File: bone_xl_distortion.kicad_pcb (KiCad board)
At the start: 2 copper layers, 35 parts, among them J1 AudioJack2, J2 AudioJack2, U1 LM358, U2 J201

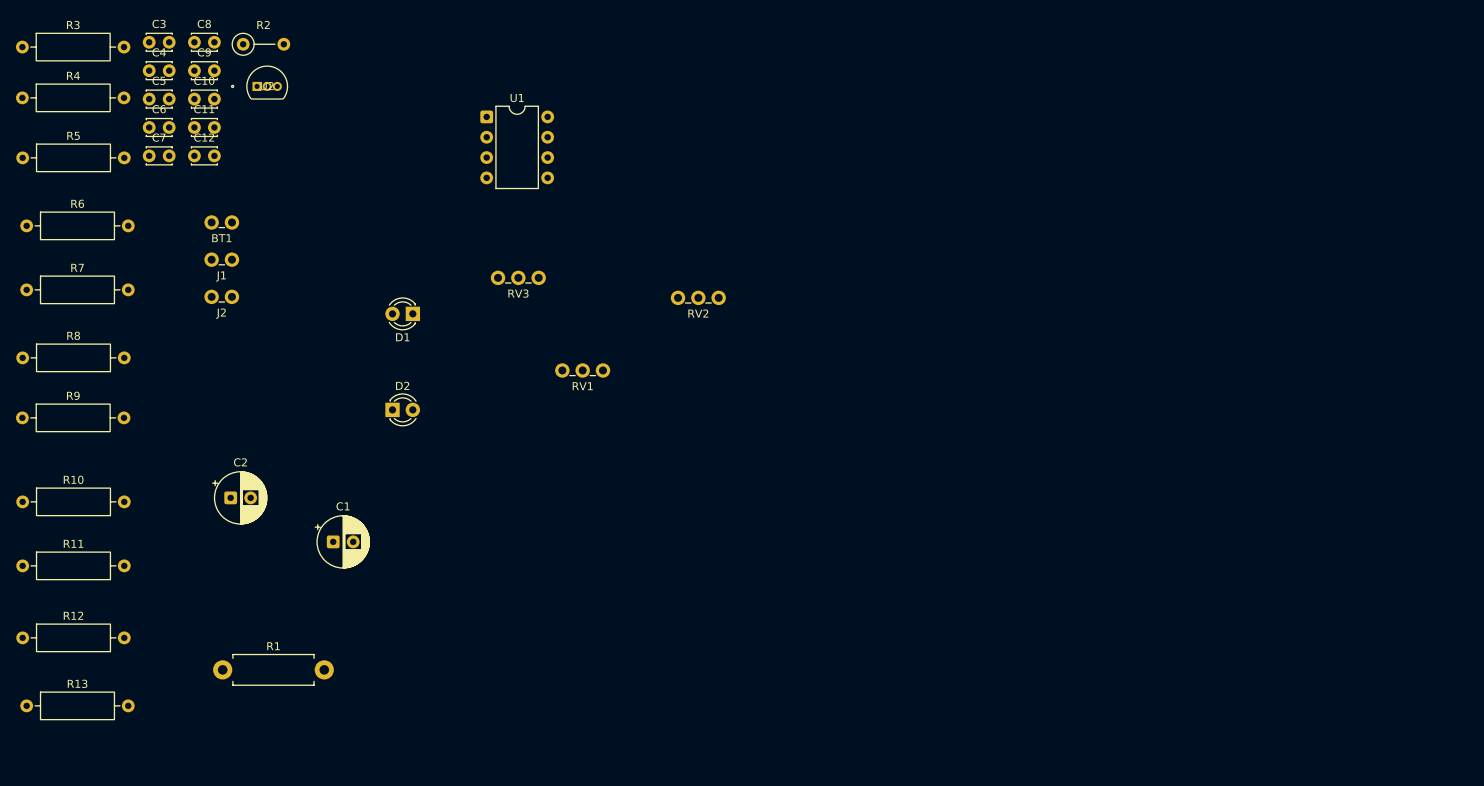
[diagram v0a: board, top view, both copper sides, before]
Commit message: finish pcb design minus silkscreen clipping and manufacturer board settings
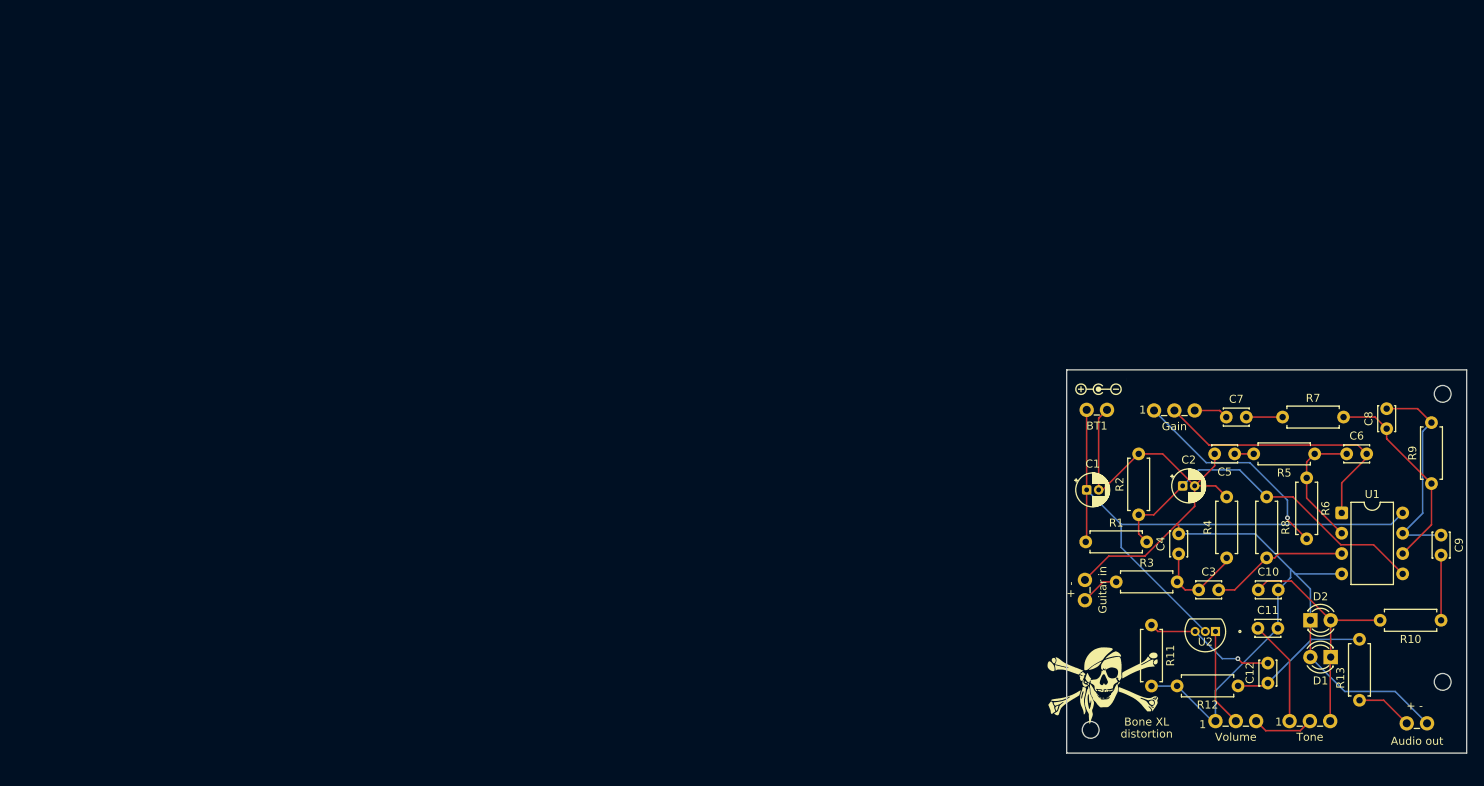
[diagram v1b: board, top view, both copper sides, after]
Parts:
- removed J1, J2: AudioJack2, standard_symbols:THT_Wire_Holes_x2
- removed RV1, RV3: 100kΩ, standard_symbols:THT_Wire_Holes_x3
- removed RV2: 10kΩ, standard_symbols:THT_Wire_Holes_x3
- added + -: Text, standard_symbols:text, F.Cu at (193.5, 110.0)
- added + -: Text, standard_symbols:text, F.Cu at (151.0, 95.0)
- added 1: Text, standard_symbols:text, F.Cu at (176.5, 112.0)
- added 1: Text, standard_symbols:text, F.Cu at (167.0, 112.3)
- added 1: Text, standard_symbols:text, F.Cu at (161.0, 71.0)
- added Audio out: AudioJack2, standard_symbols:THT_Offboard_Audio, F.Cu at (193.8, 114.4)
- added BONE XL: Text, standard_symbols:text, B.Cu at (176.5, 104.5)
- added Bone XL: Text, standard_symbols:text, F.Cu at (160.0, 112.0)
- added G***: LOGO, standard_symbols:negative_power, F.Cu at (154.0, 70.0)
- added G***: LOGO, standard_symbols:bone_logo_10mm, F.Cu at (154.5, 107.0)
- added G***: LOGO, standard_symbols:bone_logo_silk_screen, B.Cu at (175.5, 86.5)
- added G***: LOGO, standard_symbols:bone_xl_qr_silkscreen, B.Cu at (155.5, 105.0)
- added Gain: 100kΩ, standard_symbols:THT_Wire_Holes_x3, F.Cu at (163.5, 75.1)
- added Guitar in: AudioJack2, standard_symbols:THT_Offboard_Audio, F.Cu at (155.0, 95.0)
- added REF**: MountingHole_2.1mm, MountingHole:MountingHole_2.1mm, F.Cu at (197.0, 106.5)
- added REF**: MountingHole_2.1mm, MountingHole:MountingHole_2.1mm, F.Cu at (197.0, 70.5)
- added Tone: 10kΩ, standard_symbols:THT_Wire_Holes_x3, F.Cu at (180.4, 113.9)
- added Volume: 100kΩ, standard_symbols:THT_Wire_Holes_x3, F.Cu at (171.1, 113.9)
- added distortion: Text, standard_symbols:text, F.Cu at (160.0, 113.5)
- added https://github.com/delboy1978uk/bone-xl-distortion: Text, standard_symbols:text, B.Cu at (178.0, 114.0)
- added mount hole: MountingHole_2.1mm, MountingHole:MountingHole_2.1mm, F.Cu at (153.0, 112.5)
- C1, C2: footprint Capacitor_THT:CP_Radial_D6.3mm_P2.50mm -> Capacitor_THT:CP_Radial_D4.0mm_P1.50mm
- R1: footprint Resistor_THT:R_Axial_DIN0411_L9.9mm_D3.6mm_P12.70mm_Horizontal -> Resistor_THT:R_Axial_DIN0207_L6.3mm_D2.5mm_P7.62mm_Horizontal
- R10, R11, R12, R13, R3, R4, R5, R6, R7, R8, R9: footprint Resistor_THT:R_Axial_DIN0309_L9.0mm_D3.2mm_P12.70mm_Horizontal -> Resistor_THT:R_Axial_DIN0207_L6.3mm_D2.5mm_P7.62mm_Horizontal
- R2: footprint Resistor_THT:R_Axial_DIN0207_L6.3mm_D2.5mm_P5.08mm_Vertical -> Resistor_THT:R_Axial_DIN0207_L6.3mm_D2.5mm_P7.62mm_Horizontal
- moved R10 177.9 mm to (196.8, 98.8), turned to 180 degrees
- moved R9 176.3 mm to (195.6, 81.7), turned to 90 degrees
- moved R13 166.6 mm to (186.6, 108.8), turned to 90 degrees
- moved C9 166.3 mm to (196.8, 88.2), turned to -90 degrees
- moved R5 165.7 mm to (181.0, 78.0), turned to 180 degrees
- moved R6 163.1 mm to (180.0, 81.0), turned to -90 degrees
- moved R4 161.1 mm to (170.0, 91.0), turned to 90 degrees
- moved R7 157.8 mm to (177.0, 73.4)
- moved C8 156.7 mm to (190.0, 74.8), turned to 90 degrees
- moved R8 156.5 mm to (175.0, 83.4), turned to -90 degrees
- moved C6 155.1 mm to (185.0, 78.0)
- moved R3 152.2 mm to (156.2, 94.0)
- moved R12 152.0 mm to (171.4, 107.0), turned to 180 degrees
- moved C12 149.5 mm to (175.2, 106.7), turned to 90 degrees
- moved C3 148.0 mm to (166.5, 95.0)
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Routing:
- net GND: track 0.00 -> 141.7 mm
- net VCC: track 0.00 -> 76.2 mm
- net /Vref: track 0.00 -> 44.5 mm
- net Net-(C6-Pad2): track 0.00 -> 35.0 mm
- net Net-(D1-K): track 0.00 -> 30.4 mm
- net Net-(R6-Pad2): track 0.00 -> 27.1 mm, vias 0 -> 1
- net Net-(C8-Pad2): track 0.00 -> 26.5 mm
- net Net-(U1B--): track 0.00 -> 25.4 mm
- net Net-(C12-Pad1): track 0.00 -> 17.6 mm
- net Net-(U1A-+): track 0.00 -> 17.3 mm
- net Net-(U2-G): track 0.00 -> 16.5 mm, vias 0 -> 1
- net Net-(U1A--): track 0.00 -> 16.1 mm
- net Net-(C11-Pad1): track 0.00 -> 13.2 mm
- net Net-(U2-D): track 0.00 -> 12.3 mm
- net Net-(C3-Pad1): track 0.00 -> 12.1 mm
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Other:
- board outline added: 50 x 47.9 mm

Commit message: add PCBWay product marker
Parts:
- added WayWayWay: Text, standard_symbols:text, F.Cu at (179.5, 116.0)
- moved REF** 12.7 mm to (187.0, 114.4)
- moved mount hole 1.50 mm to (153.0, 114.0)
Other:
- board size 50 x 47.9 mm -> 50 x 50 mm
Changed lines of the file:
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@@
 	(footprint "MountingHole:MountingHole_2.1mm"
 		(layer "F.Cu")
-		(at 197 106.5)
+		(at 187 114.4)
 		(descr "Mounting Hole 2.1mm, no annular, generated by kicad-footprint-generator mountinghole.py")
 		(tags "mountinghole")
@@
 		(embedded_fonts no)
 	)
+	(footprint "standard_symbols:text"
+		(layer "F.Cu")
+		(at 179.5 116)
+		(property "Reference" "WayWayWay"
+			(at 0 -0.5 0)
+			(unlocked yes)
+			(layer "B.SilkS")
+			(effects
+				(font
+					(size 1 1)
+					(thickness 0.1)
+				)
+				(justify mirror)
+			)
+		)
+		(property "Value" "Text"
+			(at 0 1 0)
+			(unlocked yes)
+			(layer "F.Fab")
+			(effects
+				(font
+					(size 1 1)
+					(thickness 0.15)
+				)
+			)
+		)
+		(property "Datasheet" ""
+			(at 0 0 0)
+			(unlocked yes)
+			(layer "F.Fab")
+			(hide yes)
+			(effects
+				(font
+					(size 1 1)
+					(thickness 0.15)
+				)
+			)
+		)
+		(property "Description" ""
+			(at 0 0 0)
+			(unlocked yes)
+			(layer "F.Fab")
+			(hide yes)
+			(effects
+				(font
+					(size 1 1)
+					(thickness 0.15)
+				)
+			)
+		)
+		(attr board_only exclude_from_pos_files exclude_from_bom)
+		(fp_text user "${REFERENCE}"
+			(at 0 2.5 0)
+			(unlocked yes)
+			(layer "F.Fab")
+			(effects
+				(font
+					(size 1 1)
+					(thickness 0.15)
+				)
+			)
+		)
+		(embedded_fonts no)
+	)
 	(footprint "standard_symbols:THT_Wire_Holes_x3"
 		(layer "F.Cu")
@@
 	(footprint "MountingHole:MountingHole_2.1mm"
 		(layer "F.Cu")
-		(at 153 112.5)
+		(at 153 114)
 		(descr "Mounting Hole 2.1mm, no annular, generated by kicad-footprint-generator mountinghole.py")
 		(tags "mountinghole")
@@
 	(gr_rect
 		(start 150 67.5)
-		(end 200 115.4)
+		(end 200 117.5)
 		(stroke
 			(width 0.05)

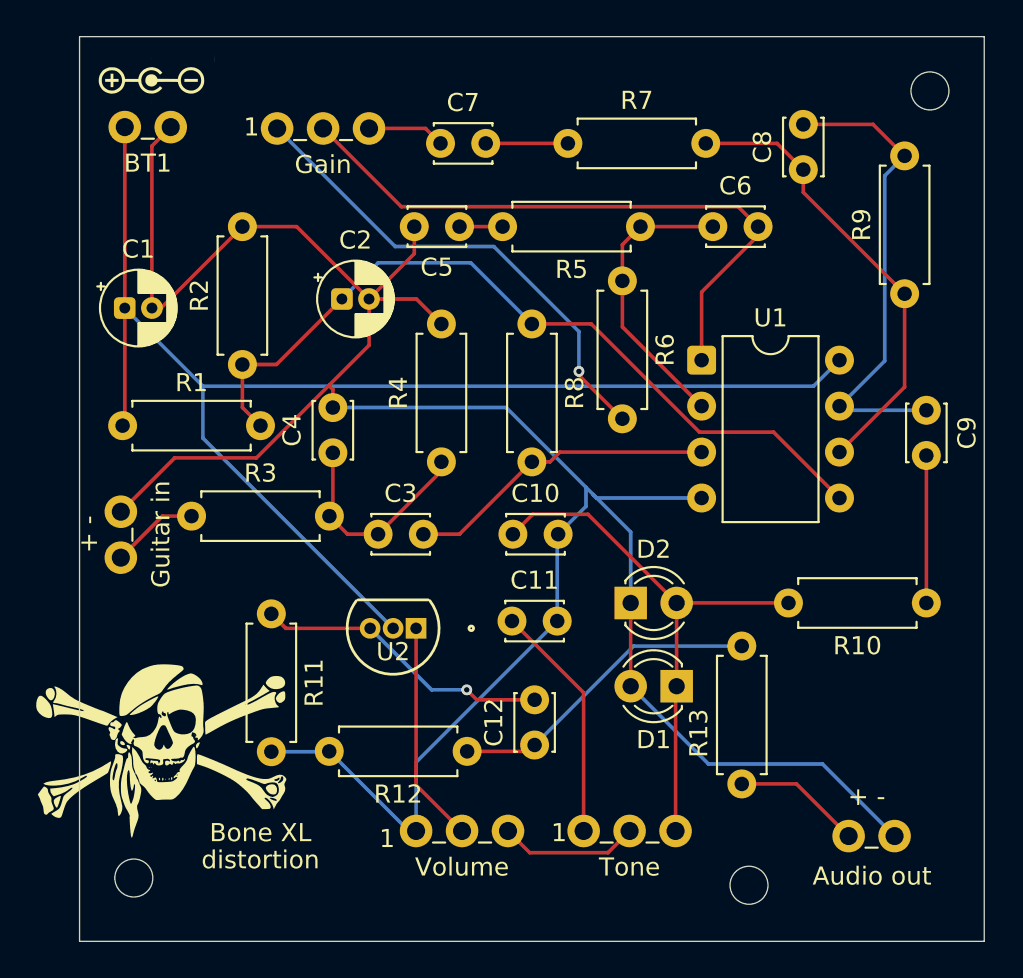
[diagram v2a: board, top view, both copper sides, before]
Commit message: add copper zones
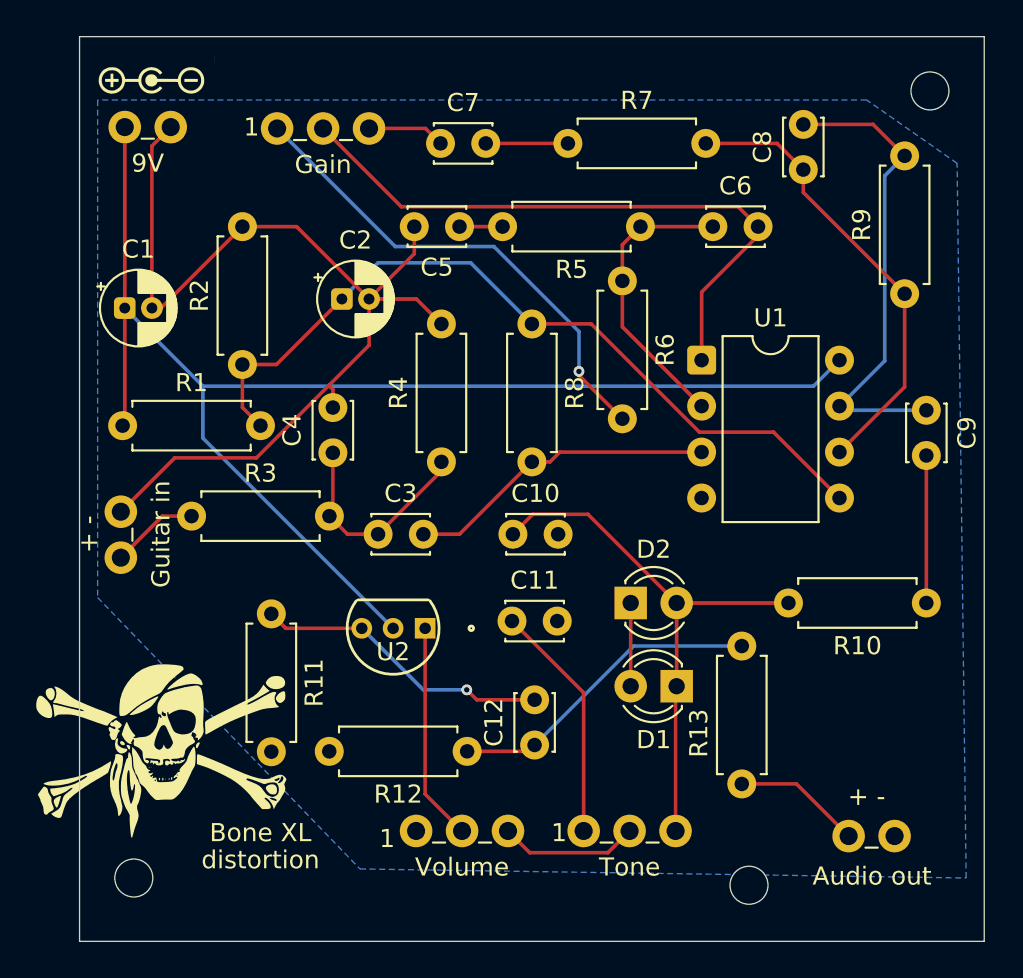
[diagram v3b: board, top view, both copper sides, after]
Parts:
- renumbered BT1 to 9V
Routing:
- net GND: track 141.7 -> 62.2 mm
- added copper zone on B.Cu, net GND
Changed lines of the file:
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@@
 		)
 		(pad "1" thru_hole rect
-			(at 0 0 180)
+			(at -0.5 0 180)
 			(size 1.143 1.143)
 			(drill 0.635)
@@
 		)
 		(pad "3" thru_hole circle
-			(at 2.54 0 180)
+			(at 3 0 180)
 			(size 1.143 1.143)
 			(drill 0.635)
@@
 		(at 153.77 75)
 		(descr "for off board components")
-		(property "Reference" "BT1"
+		(property "Reference" "9V"
 			(at 0 -0.5 0)
 			(unlocked yes)
@@
 	)
 	(segment
-		(start 184.38 93)
-		(end 178.58 93)
-		(width 0.2)
-		(layer "B.Cu")
-		(net 2)
-	)
-	(segment
-		(start 195.0446 111.6822)
-		(end 191.0614 107.699)
-		(width 0.2)
-		(layer "B.Cu")
-		(net 2)
-	)
-	(segment
-		(start 180.46 98.8)
-		(end 180.46 94.88)
-		(width 0.2)
-		(layer "B.Cu")
-		(net 2)
-	)
-	(segment
-		(start 168.6 107.6)
-		(end 176.4 99.8)
-		(width 0.2)
-		(layer "B.Cu")
-		(net 2)
-	)
-	(segment
-		(start 163.8 107)
-		(end 168.2 111.4)
-		(width 0.2)
-		(layer "B.Cu")
-		(net 2)
-	)
-	(segment
-		(start 173.58 88)
-		(end 164 88)
-		(width 0.2)
-		(layer "B.Cu")
-		(net 2)
-	)
-	(segment
-		(start 176.4 99.8)
-		(end 176.4 95.05)
-		(width 0.2)
-		(layer "B.Cu")
-		(net 2)
-	)
-	(segment
-		(start 184.759 107.699)
-		(end 180.46 103.4)
-		(width 0.2)
-		(layer "B.Cu")
-		(net 2)
-	)
-	(segment
-		(start 176.45 95)
-		(end 177.99 93.46)
-		(width 0.2)
-		(layer "B.Cu")
-		(net 2)
-	)
-	(segment
-		(start 180.46 94.88)
-		(end 178.39 92.81)
-		(width 0.2)
-		(layer "B.Cu")
-		(net 2)
-	)
-	(segment
 		(start 163.78 107.02)
 		(end 163.8 107)
@@
 	)
 	(segment
-		(start 177.99 93.46)
-		(end 177.99 92.41)
-		(width 0.2)
-		(layer "B.Cu")
-		(net 2)
-	)
-	(segment
-		(start 178.39 92.81)
-		(end 177.99 92.41)
-		(width 0.2)
-		(layer "B.Cu")
-		(net 2)
-	)
-	(segment
-		(start 168.6 111.4)
-		(end 168.6 107.6)
-		(width 0.2)
-		(layer "B.Cu")
-		(net 2)
-	)
-	(segment
-		(start 178.58 93)
-		(end 178.39 92.81)
-		(width 0.2)
-		(layer "B.Cu")
-		(net 2)
-	)
-	(segment
-		(start 191.0614 107.699)
-		(end 184.759 107.699)
-		(width 0.2)
-		(layer "B.Cu")
-		(net 2)
-	)
-	(segment
-		(start 177.99 92.41)
-		(end 173.58 88)
-		(width 0.2)
-		(layer "B.Cu")
-		(net 2)
-	)
-	(segment
 		(start 168.2 111.4)
 		(end 168.6 111.4)
@@
 	)
 	(segment
-		(start 160.6 107.02)
-		(end 163.78 107.02)
-		(width 0.2)
-		(layer "B.Cu")
-		(net 2)
-	)
-	(segment
 		(start 159 85.62)
 		(end 159 88)
@@
 	)
 	(segment
-		(start 169.46 103.6)
-		(end 171.4 103.6)
+		(start 171.4 103.6)
+		(end 169 103.6)
 		(width 0.2)
 		(layer "B.Cu")
@@
 	)
 	(segment
-		(start 166.06 100.2)
-		(end 169.46 103.6)
+		(start 169 103.6)
+		(end 165.6 100.2)
 		(width 0.2)
 		(layer "B.Cu")
@@
 	)
 	(segment
-		(start 168.6 108.86)
-		(end 171.14 111.4)
+		(start 171.14 111.4)
+		(end 169.1 109.36)
 		(width 0.2)
 		(layer "F.Cu")
@@
 	)
 	(segment
-		(start 168.6 100.2)
-		(end 168.6 108.86)
+		(start 169.1 109.36)
+		(end 169.1 100.2)
 		(width 0.2)
 		(layer "F.Cu")
 		(net 22)
 	)
+	(zone
+		(net 2)
+		(net_name "GND")
+		(layer "B.Cu")
+		(hatch edge 0.5)
+		(connect_pads
+			(clearance 0.5)
+		)
+		(min_thickness 0.25)
+		(filled_areas_thickness no)
+		(fill yes
+			(thermal_gap 0.5)
+			(thermal_bridge_width 0.5)
+		)
+		(polygon
+			(pts
+				(xy 151 71) (xy 151 98.5) (xy 165.5 113.5) (xy 199 114) (xy 198.5 74.5) (xy 193.5 71)
+			)
+		)
+	)
 	(embedded_fonts no)

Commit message: add version to silksdcreen
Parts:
- added v1.0.0: Text, standard_symbols:text, F.Cu at (196.5, 116.0)
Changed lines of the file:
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@@
+		(embedded_fonts no)
+	)
+	(footprint "standard_symbols:text"
+		(layer "F.Cu")
+		(at 196.5 116)
+		(property "Reference" "v1.0.0"
+			(at 0 -0.5 0)
+			(unlocked yes)
+			(layer "B.SilkS")
+			(effects
+				(font
+					(size 1 1)
+					(thickness 0.1)
+				)
+				(justify mirror)
+			)
+		)
+		(property "Value" "Text"
+			(at 0 1 0)
+			(unlocked yes)
+			(layer "F.Fab")
+			(effects
+				(font
+					(size 1 1)
+					(thickness 0.15)
+				)
+			)
+		)
+		(property "Datasheet" ""
+			(at 0 0 0)
+			(unlocked yes)
+			(layer "F.Fab")
+			(hide yes)
+			(effects
+				(font
+					(size 1 1)
+					(thickness 0.15)
+				)
+			)
+		)
+		(property "Description" ""
+			(at 0 0 0)
+			(unlocked yes)
+			(layer "F.Fab")
+			(hide yes)
+			(effects
+				(font
+					(size 1 1)
+					(thickness 0.15)
+				)
+			)
+		)
+		(attr board_only exclude_from_pos_files exclude_from_bom)
+		(fp_text user "${REFERENCE}"
+			(at 0 2.5 0)
+			(unlocked yes)
+			(layer "F.Fab")
+			(effects
+				(font
+					(size 1 1)
+					(thickness 0.15)
+				)
+			)
+		)
 		(embedded_fonts no)
 	)
